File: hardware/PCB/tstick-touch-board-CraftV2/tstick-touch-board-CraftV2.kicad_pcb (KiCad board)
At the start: 2 copper layers, 85.6 x 31.8 mm, 12 parts, among them J1 Conn_01x32, U1 Trill_Craft

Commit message: added new pictures of the schematics, fixed images
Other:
- board text removed: "Center X = 118.75 Y = 92.2625"
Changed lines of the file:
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@@
     (effects (font (size 1.524 1.524) (thickness 0.2032)))
-  )
-  (gr_text "Center\nX = 118.75\nY = 92.2625" (at 105.5892 93.138) (layer "Dwgs.User")
-    (effects (font (size 1 1) (thickness 0.15)) (justify left bottom))
   )
   (dimension (type aligned) (layer "Dwgs.User")

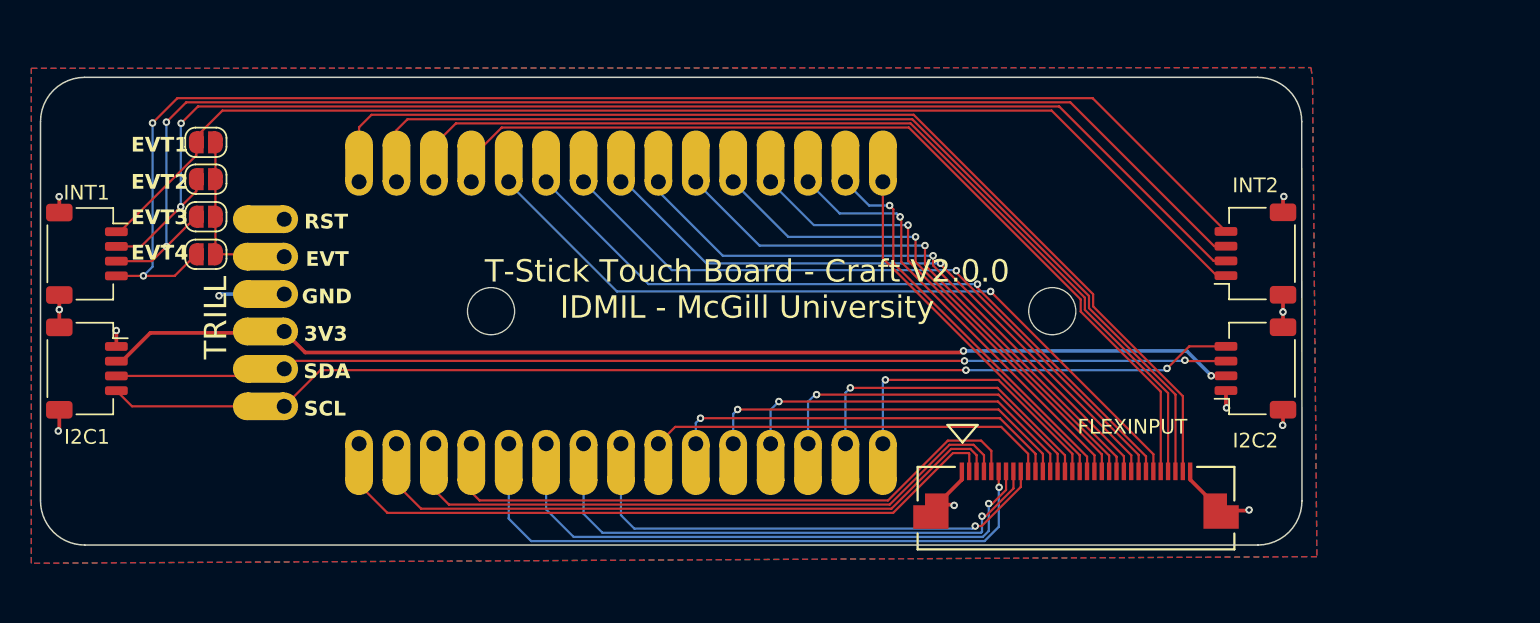
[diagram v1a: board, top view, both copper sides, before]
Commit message: added up to date gerber files, switched ground plane to hatched plane for reduced parasitic capacitance in touch board
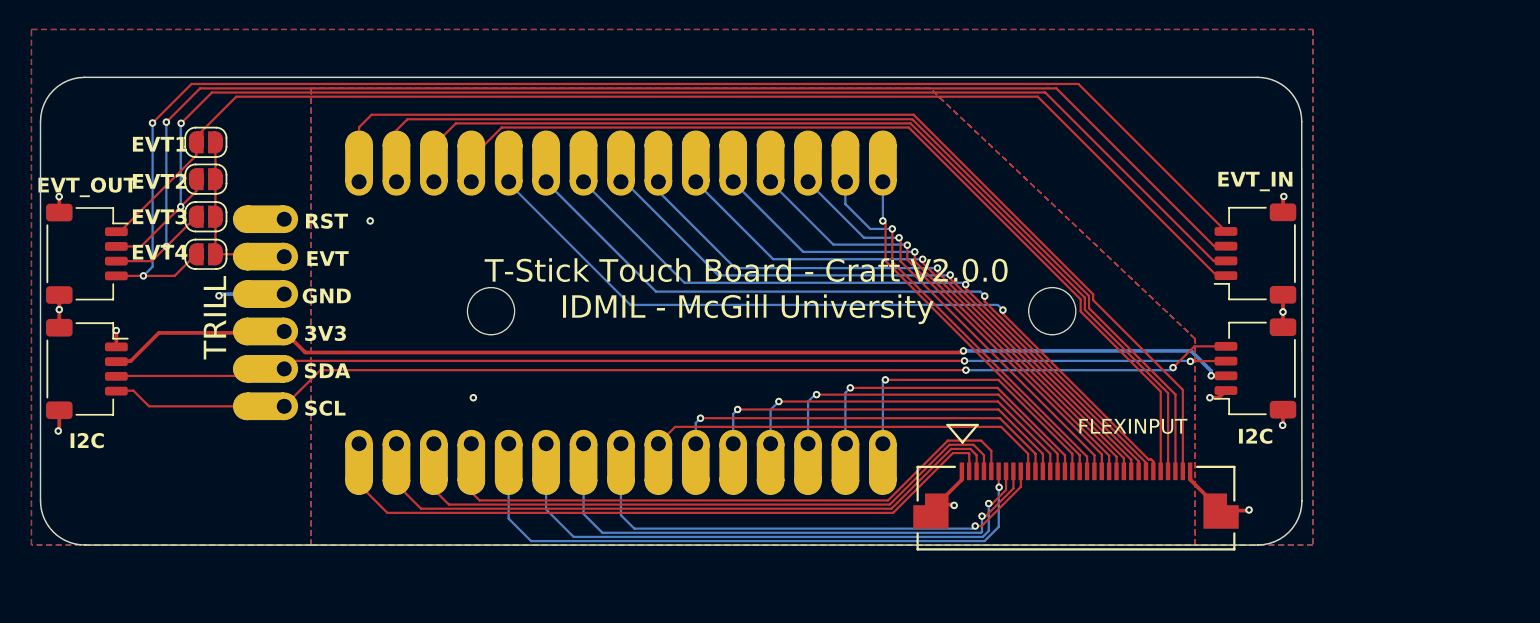
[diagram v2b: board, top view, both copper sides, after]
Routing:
- net /TOUCH17: track 29.5 -> 28.7 mm
- net /TOUCH18: track 32.3 -> 31.5 mm
- net /EVT4: track 94.0 -> 94.8 mm
- net /EVT3: track 91.7 -> 92.4 mm
- net /EVT1: track 84.1 -> 84.9 mm
- net /EVT2: track 89.2 -> 90.0 mm
- net /TOUCH20: track 37.6 -> 37.0 mm
- net /TOUCH19: track 34.9 -> 34.2 mm
- net GND: track 25.0 -> 25.1 mm, vias 11 -> 13
- net /TOUCH15: vias 0 -> 1
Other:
- board text added: "EVT_IN"
- board text added: "EVT_OUT"
- board text added: "I2C"

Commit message: fixed errors in schematic, added support for V1 Trill boards in v2 board design, changed headers to vertical headers in touch board
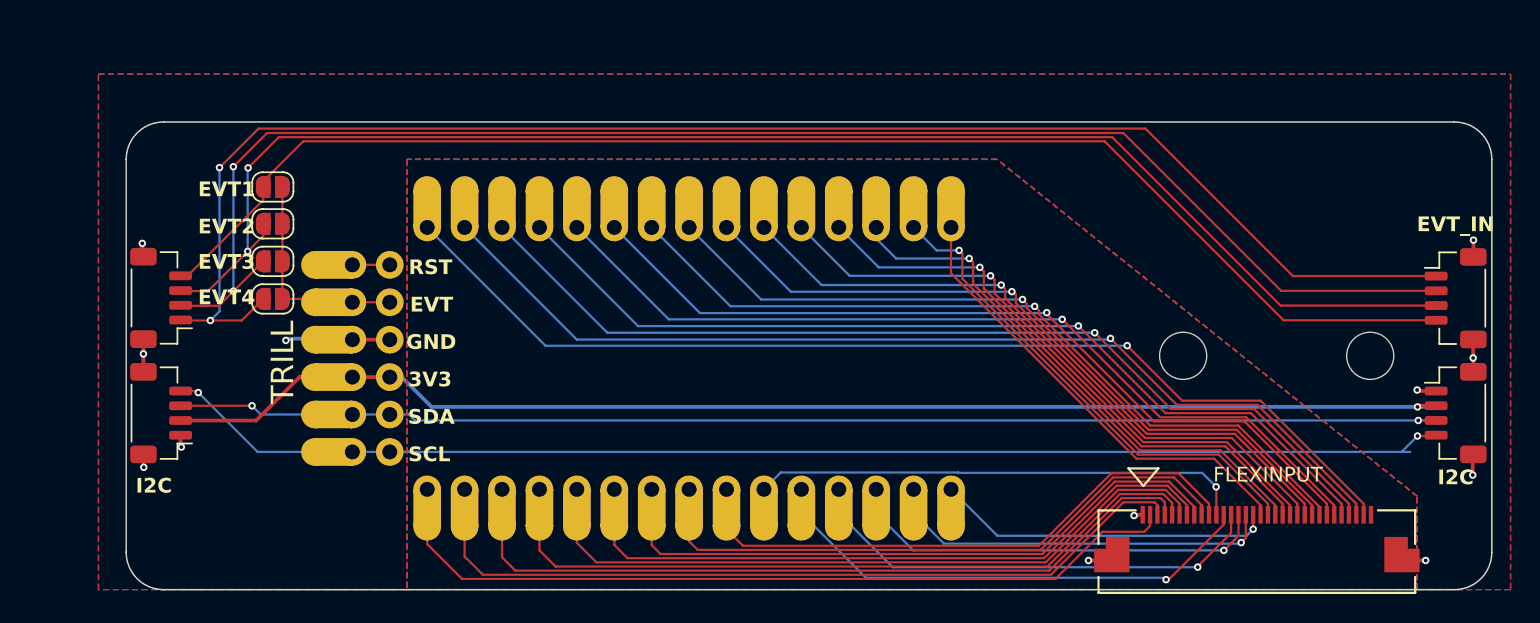
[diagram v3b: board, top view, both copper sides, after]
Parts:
- I2C1, I2C2, INT1, INT2: footprint Connector_JST:JST_SH_SM04B-SRSS-TB_1x04-1MP_P1.00mm_Horizontal -> JST Connectors:JST_SH_BM04B-SRSS-TB_1x04-1MP_P1.00mm_Vertical
- moved H2 47.1 mm to (210.2, 97.2)
- moved H1 21.8 mm to (222.9, 97.2)
- moved I2C2 13.9 mm to (228.7, 101.0), turned to -90 degrees
- moved INT2 13.9 mm to (228.7, 93.2), turned to -90 degrees
- moved J1 12.6 mm to (215.2, 110.4)
- moved U1 5.93 mm to (176.6, 97.3)
- moved I2C1 5.86 mm to (140.8, 101.0), turned to 90 degrees
- moved INT1 5.86 mm to (140.8, 93.2), turned to 90 degrees
- moved JP1 5.46 mm to (148.4, 85.7)
- moved JP2 5.46 mm to (148.4, 88.2)
- moved JP3 5.46 mm to (148.4, 90.7)
- moved JP4 5.46 mm to (148.4, 93.3)
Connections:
- INT1 pad 1: /EVT1 -> /EVT4
- INT1 pad 2: /EVT2 -> /EVT3
- INT1 pad 3: /EVT3 -> /EVT2
- INT1 pad 4: /EVT4 -> /EVT1
- INT2 pad 1: /EVT1 -> /EVT4
- INT2 pad 2: /EVT2 -> /EVT3
- INT2 pad 3: /EVT3 -> /EVT2
- INT2 pad 4: /EVT4 -> /EVT1
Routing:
- net /SDA: track 75.8 -> 89.0 mm
- net /SCL: track 77.5 -> 90.1 mm
- net /TOUCH8: track 27.1 -> 39.6 mm
- net /EVT4: track 94.8 -> 104.4 mm
- net /EVT2: track 90.0 -> 99.6 mm
- net /EVT3: track 92.4 -> 102.1 mm
- net /EVT1: track 84.9 -> 94.5 mm
- net /TOUCH1: track 45.3 -> 54.9 mm
- net /TOUCH2: track 43.5 -> 53.0 mm
- net +3V3: track 77.7 -> 87.1 mm, vias 2 -> 1
- net /TOUCH10: track 25.2 -> 34.4 mm
- net /TOUCH3: track 41.8 -> 50.6 mm
- net /TOUCH0: track 47.4 -> 56.0 mm
- net /TOUCH11: track 23.7 -> 32.0 mm
- net /TOUCH17: track 28.7 -> 36.8 mm
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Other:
- board size 85.6 x 31.8 mm -> 92.7 x 31.8 mm
- board text added: "T-Stick Touch Board - Craft V2.0.0 IDMIL - McGill University Albert Niyonsenga"
- board text removed: "EVT_OUT"
- board text removed: "T-Stick Touch Board - Craft V2.0.0 IDMIL - McGill University"
